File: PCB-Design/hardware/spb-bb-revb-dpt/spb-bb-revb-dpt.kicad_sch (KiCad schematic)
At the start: 191 parts, among them J1 DC+, J10 U.FL H2, J11 U.FL L2, J12 V_ISO,HS in, J13 V_ISO,LS in, J14 CTRL2, J15 MMCX VDS L3, J16 U.FL H3, J17 U.FL L3, J18 MMCX VDS L4, J19 U.FL H4, J2 DC-, J20 U.FL L4, J21 AC, J3 V_ISO,HS in, J4 V_ISO,LS in, J5 CTRL1, J6 MMCX VDS L1, J7 U.FL H1, J8 U.FL L1, J9 MMCX VDS L2, Q1 EPC2361, Q2 EPC2361, Q3 EPC2361, Q4 EPC2361, Q5 EPC2361, Q6 EPC2361, Q7 EPC2361, Q8 EPC2361, U1 2EDF7275K, U2 2EDF7275K

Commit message: DPT board: R_ON 1.5 Ohm and -1.9 V gate off-bias; SPICE shunt inductance fixed
- SPICE: the UFCS shunt's 120 pH was written as Lser on a resistor, which LTspice
  rejects and ignores; now a separate inductor. Part body ESLs added to the gate
  network (0603 R_G / R_ON / R_OFF 0.4 nH, D_OFF 1 nH); gate off level -1.9 V
  (V_ISO 7 V with the 5.1 V Zener); the lumped-gate case had been commented out
- with the corrected model R_ON 1.0 Ohm gives a 105 V HS V_DS peak: R_ON 1.5 Ohm
  (R7/R9/R26/R28, Yageo RC0603FR-071R5L, R_G,on 3.5 Ohm) gives 92.9 V, E_on 125 uJ,
  E_off 20 uJ; V_GS bump on the held-off FET -0.50 ... -0.76 V (was +1.4 V at 0 V off)
- DPT_measurement_setup: gate-drive settings (V_ISO 7 V, R_ON, one PWM source and
  equal cables for U1/U2); review document 10.2
- DRC 0/0 (fresh load too), sch = PCB, no 3D collisions, 36 test points

Co-Authored-By: Claude Opus 5.5 <noreply@anthropic.com>
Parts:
- R26, R28, R7, R9: value 1R0 1% -> 1R5 1%; MPN 1.0R 0603 1% (Yageo RC0603FR-071RL) -> 1.5R 0603 1% (Yageo RC0603FR-071R5L)
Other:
- note added: "R_ON 1.5 R, R_OFF 0 R (jumper), R_G 0.5 R per transistor, 10 k gate pull-down at the star to the Kelvin net"
- note removed: "R_ON 1.0 R, R_OFF 0 R (jumper), R_G 0.5 R per transistor, 10 k gate pull-down at the star to the Kelvin net"
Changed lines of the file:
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@@
  (text "NTC on the control side (board temperature at the driver)" (at 33.02 262.89 0) (effects (font (size 1.27 1.27)) (justify left bottom)))
  (text "SLDON = GNDI: input-side LDO on" (at 139.70 248.92 0) (effects (font (size 1.27 1.27)) (justify left bottom)))
- (text "R_ON 1.0 R, R_OFF 0 R (jumper), R_G 0.5 R per transistor, 10 k gate pull-down at the star to the Kelvin net" (at 139.70 251.46 0) (effects (font (size 1.27 1.27)) (justify left bottom)))
+ (text "R_ON 1.5 R, R_OFF 0 R (jumper), R_G 0.5 R per transistor, 10 k gate pull-down at the star to the Kelvin net" (at 139.70 251.46 0) (effects (font (size 1.27 1.27)) (justify left bottom)))
  (text "BLOCK 2" (at 436.88 190.50 0) (effects (font (size 1.80 1.80) bold) (justify left bottom)))
  (text "SLDON = GNDI: input-side LDO on" (at 546.10 248.92 0) (effects (font (size 1.27 1.27)) (justify left bottom)))
- (text "R_ON 1.0 R, R_OFF 0 R (jumper), R_G 0.5 R per transistor, 10 k gate pull-down at the star to the Kelvin net" (at 546.10 251.46 0) (effects (font (size 1.27 1.27)) (justify left bottom)))
+ (text "R_ON 1.5 R, R_OFF 0 R (jumper), R_G 0.5 R per transistor, 10 k gate pull-down at the star to the Kelvin net" (at 546.10 251.46 0) (effects (font (size 1.27 1.27)) (justify left bottom)))
  (text "GATE SUPPLY ISLANDS: external isolated supply (one HS, one LS, split per block) -> WE-CNSW -> 5.1 V Zener VDD-S, 150 R bias S-VEE: V_GS,on = +5.1 V, V_GS,off = -(V_ISO - 5.1 V)" (at 25.40 266.70 0) (effects (font (size 2.00 2.00) bold) (justify left bottom)))
  (text "J3 / L1: HS block 1" (at 33.02 314.96 0) (effects (font (size 1.50 1.50)) (justify left bottom)))
@@
  (symbol (lib_id "Device:R") (at 604.52 215.90 90) (unit 1) (in_bom yes) (on_board yes) (dnp no)
   (property "Reference" "R26" (at 604.52 213.10 90) (effects (font (size 1.27 1.27))))
-  (property "Value" "1R0 1%" (at 604.52 218.70 90) (effects (font (size 1.27 1.27))))
+  (property "Value" "1R5 1%" (at 604.52 218.70 90) (effects (font (size 1.27 1.27))))
   (property "Footprint" "Resistor_SMD:R_0603_1608Metric" (at 604.52 215.90 90) (effects (font (size 1.27 1.27)) hide))
   (property "Datasheet" "~" (at 604.52 215.90 90) (effects (font (size 1.27 1.27)) hide))
-  (property "MPN" "1.0R 0603 1% (Yageo RC0603FR-071RL)" (at 604.52 215.90 90) (effects (font (size 1.27 1.27)) hide))
-  (property "Description" "1R0 1% (R_ON,A)" (at 604.52 215.90 90) (effects (font (size 1.27 1.27)) hide))
+  (property "MPN" "1.5R 0603 1% (Yageo RC0603FR-071R5L)" (at 604.52 215.90 90) (effects (font (size 1.27 1.27)) hide))
+  (property "Description" "1R5 1% (R_ON,A)" (at 604.52 215.90 90) (effects (font (size 1.27 1.27)) hide))
   (pin "1") (pin "2")
   (instances (project "spb-bb-revb-dpt" (path "/e62a99d0-4c10-5aed-840f-6353566af670" (reference "R26") (unit 1)))))
@@
  (symbol (lib_id "Device:R") (at 604.52 226.06 90) (unit 1) (in_bom yes) (on_board yes) (dnp no)
   (property "Reference" "R28" (at 604.52 223.26 90) (effects (font (size 1.27 1.27))))
-  (property "Value" "1R0 1%" (at 604.52 228.86 90) (effects (font (size 1.27 1.27))))
+  (property "Value" "1R5 1%" (at 604.52 228.86 90) (effects (font (size 1.27 1.27))))
   (property "Footprint" "Resistor_SMD:R_0603_1608Metric" (at 604.52 226.06 90) (effects (font (size 1.27 1.27)) hide))
   (property "Datasheet" "~" (at 604.52 226.06 90) (effects (font (size 1.27 1.27)) hide))
-  (property "MPN" "1.0R 0603 1% (Yageo RC0603FR-071RL)" (at 604.52 226.06 90) (effects (font (size 1.27 1.27)) hide))
-  (property "Description" "1R0 1% (R_ON,B)" (at 604.52 226.06 90) (effects (font (size 1.27 1.27)) hide))
+  (property "MPN" "1.5R 0603 1% (Yageo RC0603FR-071R5L)" (at 604.52 226.06 90) (effects (font (size 1.27 1.27)) hide))
+  (property "Description" "1R5 1% (R_ON,B)" (at 604.52 226.06 90) (effects (font (size 1.27 1.27)) hide))
   (pin "1") (pin "2")
   (instances (project "spb-bb-revb-dpt" (path "/e62a99d0-4c10-5aed-840f-6353566af670" (reference "R28") (unit 1)))))
@@
  (symbol (lib_id "Device:R") (at 198.12 215.90 90) (unit 1) (in_bom yes) (on_board yes) (dnp no)
   (property "Reference" "R7" (at 198.12 213.10 90) (effects (font (size 1.27 1.27))))
-  (property "Value" "1R0 1%" (at 198.12 218.70 90) (effects (font (size 1.27 1.27))))
+  (property "Value" "1R5 1%" (at 198.12 218.70 90) (effects (font (size 1.27 1.27))))
   (property "Footprint" "Resistor_SMD:R_0603_1608Metric" (at 198.12 215.90 90) (effects (font (size 1.27 1.27)) hide))
   (property "Datasheet" "~" (at 198.12 215.90 90) (effects (font (size 1.27 1.27)) hide))
-  (property "MPN" "1.0R 0603 1% (Yageo RC0603FR-071RL)" (at 198.12 215.90 90) (effects (font (size 1.27 1.27)) hide))
-  (property "Description" "1R0 1% (R_ON,A)" (at 198.12 215.90 90) (effects (font (size 1.27 1.27)) hide))
+  (property "MPN" "1.5R 0603 1% (Yageo RC0603FR-071R5L)" (at 198.12 215.90 90) (effects (font (size 1.27 1.27)) hide))
+  (property "Description" "1R5 1% (R_ON,A)" (at 198.12 215.90 90) (effects (font (size 1.27 1.27)) hide))
   (pin "1") (pin "2")
   (instances (project "spb-bb-revb-dpt" (path "/e62a99d0-4c10-5aed-840f-6353566af670" (reference "R7") (unit 1)))))
@@
  (symbol (lib_id "Device:R") (at 198.12 226.06 90) (unit 1) (in_bom yes) (on_board yes) (dnp no)
   (property "Reference" "R9" (at 198.12 223.26 90) (effects (font (size 1.27 1.27))))
-  (property "Value" "1R0 1%" (at 198.12 228.86 90) (effects (font (size 1.27 1.27))))
+  (property "Value" "1R5 1%" (at 198.12 228.86 90) (effects (font (size 1.27 1.27))))
   (property "Footprint" "Resistor_SMD:R_0603_1608Metric" (at 198.12 226.06 90) (effects (font (size 1.27 1.27)) hide))
   (property "Datasheet" "~" (at 198.12 226.06 90) (effects (font (size 1.27 1.27)) hide))
-  (property "MPN" "1.0R 0603 1% (Yageo RC0603FR-071RL)" (at 198.12 226.06 90) (effects (font (size 1.27 1.27)) hide))
-  (property "Description" "1R0 1% (R_ON,B)" (at 198.12 226.06 90) (effects (font (size 1.27 1.27)) hide))
+  (property "MPN" "1.5R 0603 1% (Yageo RC0603FR-071R5L)" (at 198.12 226.06 90) (effects (font (size 1.27 1.27)) hide))
+  (property "Description" "1R5 1% (R_ON,B)" (at 198.12 226.06 90) (effects (font (size 1.27 1.27)) hide))
   (pin "1") (pin "2")
   (instances (project "spb-bb-revb-dpt" (path "/e62a99d0-4c10-5aed-840f-6353566af670" (reference "R9") (unit 1)))))

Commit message: DPT board: loop test points, PWM chokes removed, silk audit; documents updated
- layer-and-PWM review: PWM_H/PWM_L common-mode chokes removed (driver input isolated;
  choke leakage L + 100 pF input filter rings, delay can differ U1/U2); DIS, 12 V, NTC
  keep theirs; bring-up notes (SW bus, PWM checks, L2 return) in DPT_measurement_setup
- bring-up test points as through-hole loop points (1.0 mm hole, 1.8 mm pad, Keystone
  5000 / Adafruit 3825, lab-fitted) where a hole fits: 13 (DC+, DC-, SW, driver
  islands); SMD pad fallback elsewhere; spring pads placed first: 38 labelled points
- silk: drilled holes are silk obstacles (53 labels had sat on vias); new
  scripts/check_silk.py audit (holes, mask openings, overlaps, edge, size): 0 problems;
  board titles and CELL labels found free spots; "DESIGNED BY CLAUDE" on top
- schematic generator follows the choke change; BOM line for the loop test points
- paper / digest / deck: text on the PWM inputs, renders of the final board

DRC 0/0 (fresh load too), silk audit 0, sch = PCB (86 nets, 183 parts), no 3D
collisions; paper 6 pp, digest 5 pp, deck 54 slides.

Co-Authored-By: Claude Opus 5.5 <noreply@anthropic.com>
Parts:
- removed L10, L11, L12, L13: WE-CNSW 744232601, spb_fab:L_CommonMode_Wurth_WE-CNSW-1206, symbol spb_fab:WE-CNSW
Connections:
- net C_PWMH2 is gone; now on net PWM_H2: J14.2 (Pin_2)
- net C_PWML2 is gone; now on net PWM_L2: J14.4 (Pin_4)
- net C_RTN_PWMH2 is gone; now on net GNDI2: J14.1 (Pin_1)
- net C_RTN_PWML2 is gone; now on net GNDI2: J14.3 (Pin_3)
- net 12V_CM1: now also L4.2; no longer L6.2
- net 12V_CM2: now also L9.2
- net C_12V1: now also L4.1; no longer L6.1
- net C_12V2: now also L9.1
- net C_DIS1: now also L3.4; no longer L5.4
- net C_DIS2: now also L8.4
- net C_NTC1: now also L5.4; no longer L7.4
- net C_RTN_12V1: now also L4.4; no longer L6.4
- net C_RTN_12V2: now also L9.4
- net C_RTN_DIS1: now also L3.1; no longer L5.1
- net C_RTN_DIS2: now also L8.1
- net C_RTN_NTC1: now also L5.1; no longer L7.1
- net DIS1: now also L3.3; no longer L5.3
- net DIS2: now also L8.3
- net GNDI1: now also J5.1 (Pin_1), J5.3 (Pin_3); no longer L6.3, L7.2
- net GNDI2: now also L8.2, L9.3
- net NTC: now also L5.3; no longer L7.3
- net PWM_H1: now also J5.2 (Pin_2); no longer L3.3
- net PWM_L1: now also J5.4 (Pin_4); no longer L4.2
- net VDDA2: now also L6.4; no longer L8.4
- net VDDB2: now also L7.4; no longer L9.4
- net VEEA2: now also L6.1; no longer L8.1
- net VEEB2: now also L7.1; no longer L9.1
- net VINA_N2: now also L6.2; no longer L8.2
- net VINA_P2: now also L6.3; no longer L8.3
- net VINB_N2: now also L7.2; no longer L9.2
- net VINB_P2: now also L7.3; no longer L9.3
- removed net C_PWMH1: J5.2 (Pin_2), L3.4
- removed net C_PWML1: J5.4 (Pin_4), L4.1
- removed net C_RTN_PWMH1: J5.1 (Pin_1), L3.1
- removed net C_RTN_PWML1: J5.3 (Pin_3), L4.4
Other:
- note added: "Block suffix 1/2 on every driver-side net (GNDI1, VDDA2, ...). Control side (CTRLx 2 x 5 header): PWM_H and PWM_L straight to the 47 R / 100 pF input filters (returns to GNDI, no choke: no added delay); DIS, 12 V and (block 1) NTC each with their own return C_RTN_* through one WE-CNSW common-mode choke per pair; 12 V then through a ferrite bead. The control side is a top-layer-only area with a 12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"
- note added: "GATE DRIVER BLOCKS: control header (chokes on DIS / 12 V / NTC), 2EDF7275K input filters, R_ON / D + R_OFF, star, R_G per transistor (block 1 drives Q1-Q4, block 2 drives Q5-Q8)"
- note added: "J12 / L6: HS block 2"
- note added: "J13 / L7: LS block 2"
- note removed: "Block suffix 1/2 on every driver-side net (GNDI1, VDDA2, ...). Control side (CTRLx 2 x 5 header): PWM_H, PWM_L, DIS, 12 V and (block 1) NTC each with their own return C_RTN_* through one WE-CNSW common-mode choke per pair; 12 V then through a ferrite bead. The control side is a top-layer-only area with a 1200 V barrier (4 mm outer, 3 mm L2) to all power copper; see reports/pcb-rules/PCB_rules_and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"
- note removed: "GATE DRIVER BLOCKS: control header with common-mode chokes, 2EDF7275K input filters, R_ON / D + R_OFF, star, R_G per transistor (block 1 drives Q1-Q4, block 2 drives Q5-Q8)"
- note removed: "J12 / L8: HS block 2"
- note removed: "J13 / L9: LS block 2"
- moved on the sheet: L6, L7, L8, L9

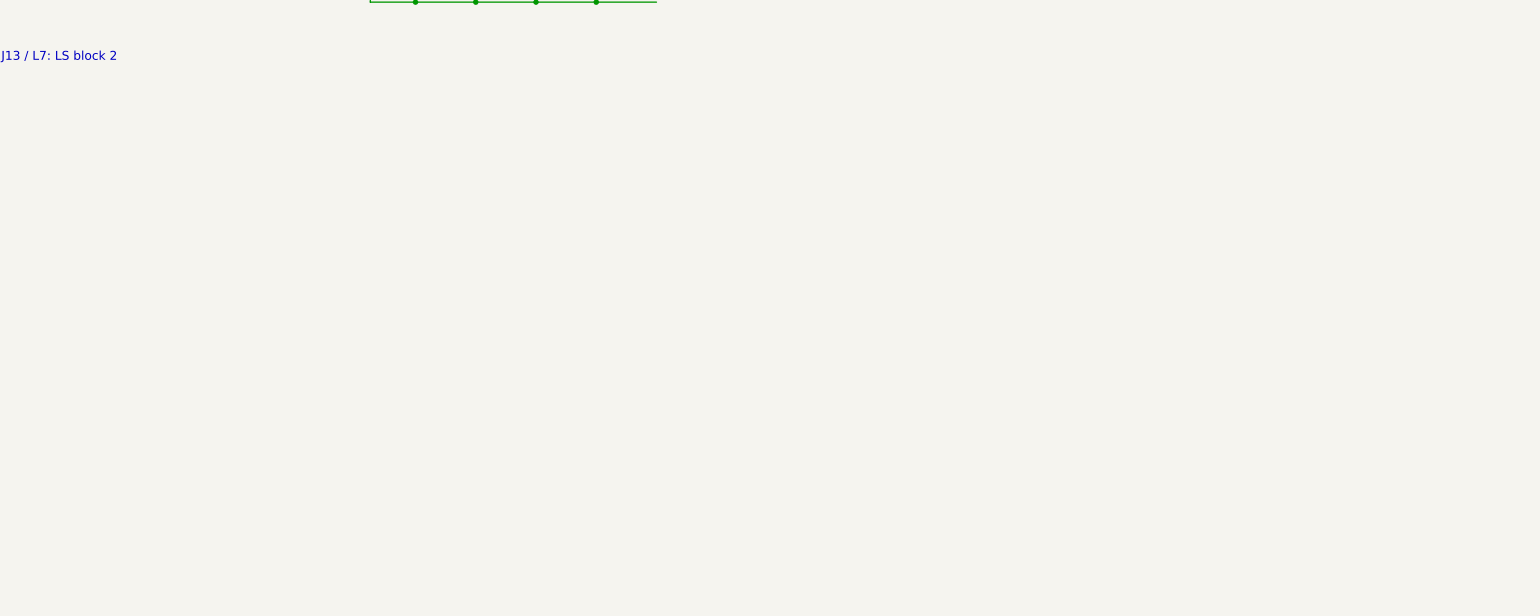
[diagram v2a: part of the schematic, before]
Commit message: DPT board: through-hole loop test points (Adafruit 3825), silkscreen fix
- 13 loop test points as plated holes (1.02 mm drill, 1.8 mm pad) for the
  Adafruit 3825 / Keystone 5000 red loop; 3D model, BOM line and
  Connector:TestPoint symbols in the schematic (TEST POINTS section)
- remaining points as SMD pads, spring-probe pads for V_GS / V_DS
- silkscreen: net names next to the test points on both sides, group labels
  for rows of passives, leader lines, protected FET/connector labels,
  "DESIGNED BY CLAUDE"; new silk audit (check_silk.py: 0 problems) and
  top/bottom silk views (render_silk_view.py)
- fab: retry when an output file is locked by another process (Windows);
  deck: same for slide images
- fab, JLC, paper, digest and slides regenerated; DRC 0/0, 3D no collisions

Co-Authored-By: Claude Opus 5.5 <noreply@anthropic.com>
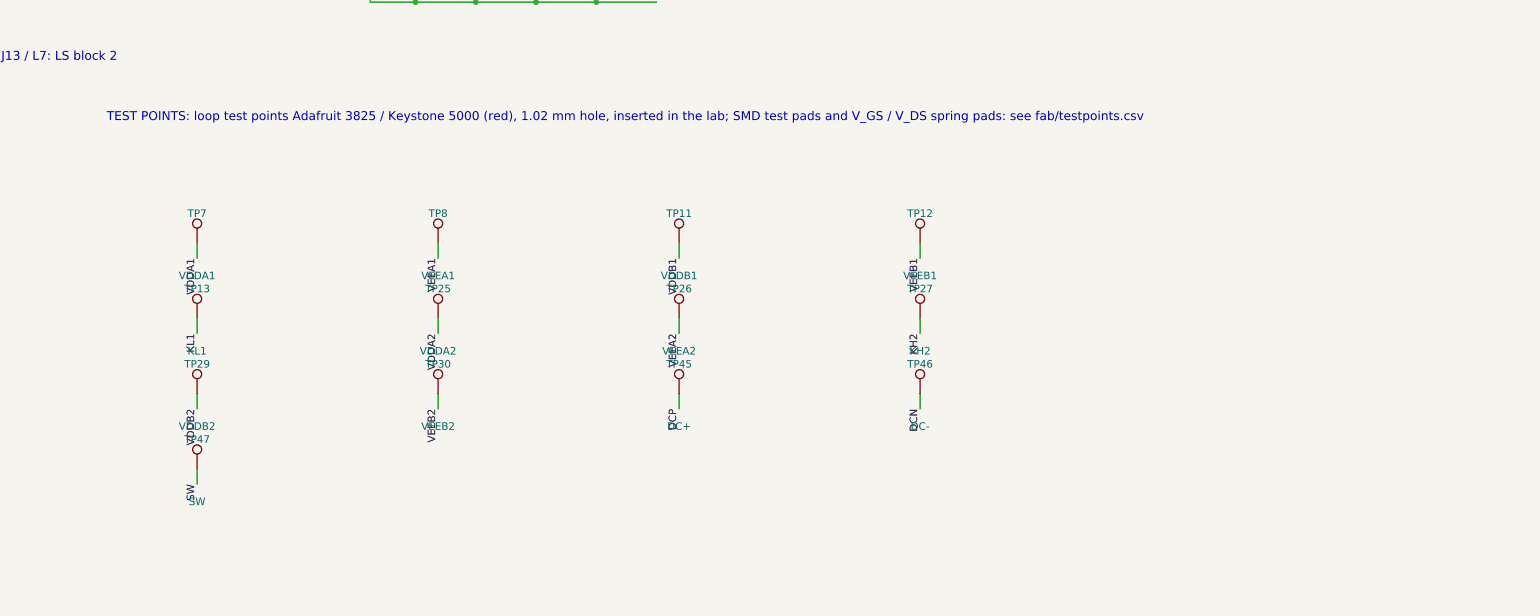
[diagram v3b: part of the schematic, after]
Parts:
- added TP11: VDDB1, spb_fab:TestPoint_Keystone5000_Adafruit3825, symbol Connector:TestPoint
- added TP12: VEEB1, spb_fab:TestPoint_Keystone5000_Adafruit3825, symbol Connector:TestPoint
- added TP13: KL1, spb_fab:TestPoint_Keystone5000_Adafruit3825, symbol Connector:TestPoint
- added TP25: VDDA2, spb_fab:TestPoint_Keystone5000_Adafruit3825, symbol Connector:TestPoint
- added TP26: VEEA2, spb_fab:TestPoint_Keystone5000_Adafruit3825, symbol Connector:TestPoint
- added TP27: KH2, spb_fab:TestPoint_Keystone5000_Adafruit3825, symbol Connector:TestPoint
- added TP29: VDDB2, spb_fab:TestPoint_Keystone5000_Adafruit3825, symbol Connector:TestPoint
- added TP30: VEEB2, spb_fab:TestPoint_Keystone5000_Adafruit3825, symbol Connector:TestPoint
- added TP45: DC+, spb_fab:TestPoint_Keystone5000_Adafruit3825, symbol Connector:TestPoint
- added TP46: DC-, spb_fab:TestPoint_Keystone5000_Adafruit3825, symbol Connector:TestPoint
- added TP47: SW, spb_fab:TestPoint_Keystone5000_Adafruit3825, symbol Connector:TestPoint
- added TP7: VDDA1, spb_fab:TestPoint_Keystone5000_Adafruit3825, symbol Connector:TestPoint
- added TP8: VEEA1, spb_fab:TestPoint_Keystone5000_Adafruit3825, symbol Connector:TestPoint
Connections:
- net DCN: now also TP46.1
- net DCP: now also TP45.1
- net KH2: now also TP27.1
- net KL1: now also TP13.1
- net SW: now also TP47.1
- net VDDA1: now also TP7.1
- net VDDA2: now also TP25.1
- net VDDB1: now also TP11.1
- net VDDB2: now also TP29.1
- net VEEA1: now also TP8.1
- net VEEA2: now also TP26.1
- net VEEB1: now also TP12.1
- net VEEB2: now also TP30.1
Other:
- note added: "TEST POINTS: loop test points Adafruit 3825 / Keystone 5000 (red), 1.02 mm hole, inserted in the lab; SMD test pads and V_GS / V_DS spring pads: see fab/testpoints.csv"
